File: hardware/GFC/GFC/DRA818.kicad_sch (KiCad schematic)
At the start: 24 parts, among them J3 USB Sound Card Connection, Q2 DMN67D8LW-13, Q3 Q_NPN_BCE, SW1 H/L_DIP_SW

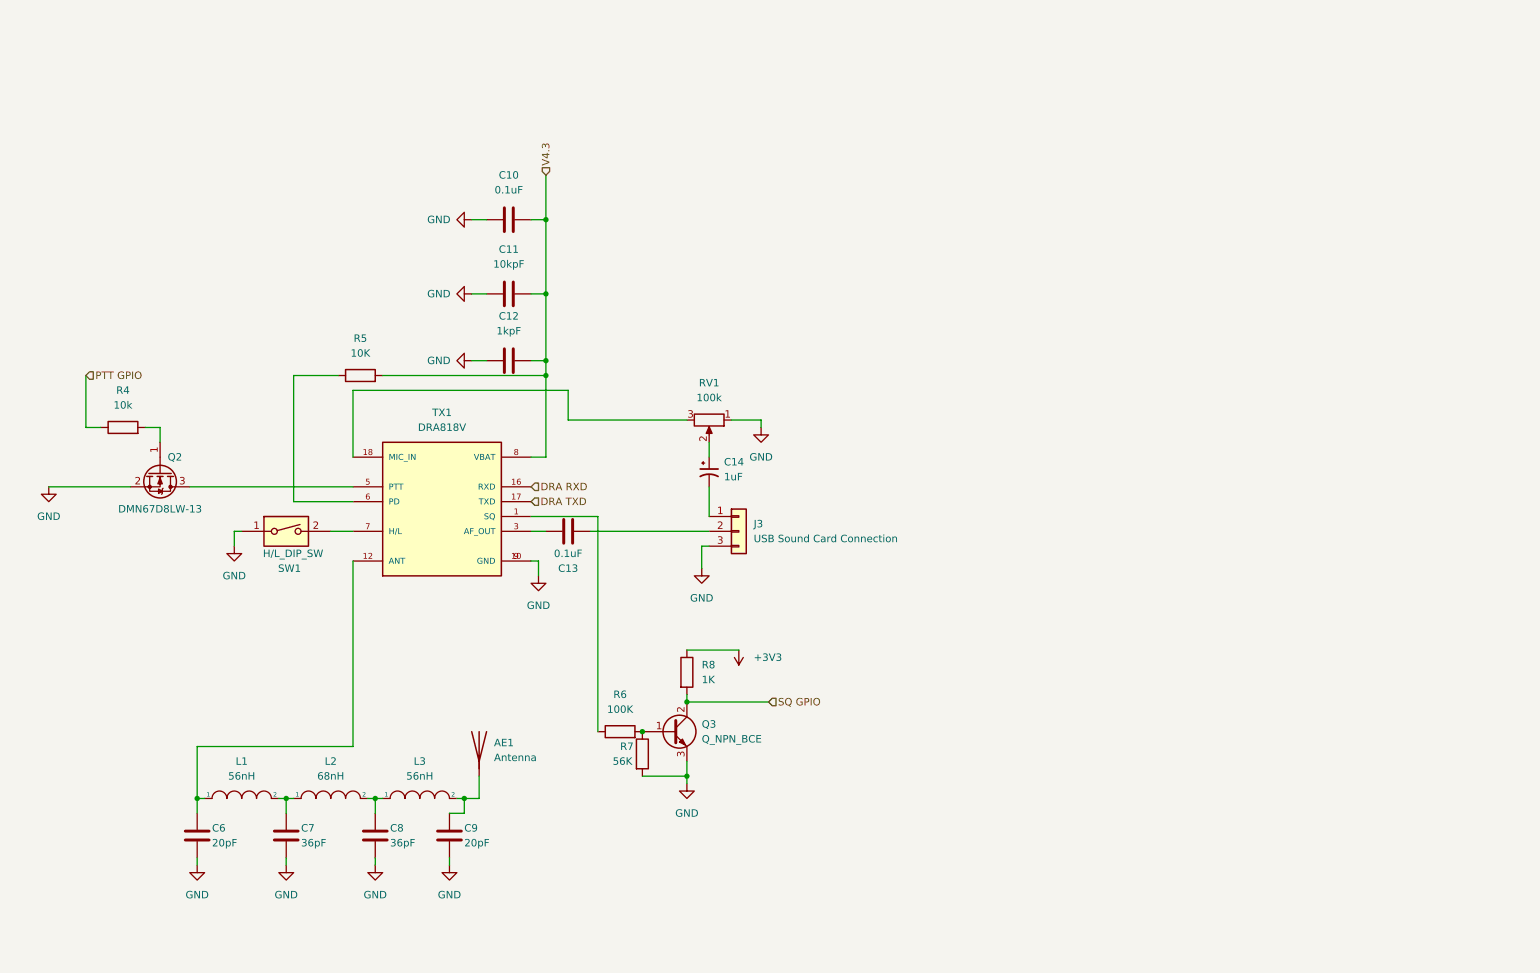
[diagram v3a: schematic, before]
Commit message: Schematic Update - ADC/DAC & GPIO Config EEPROM
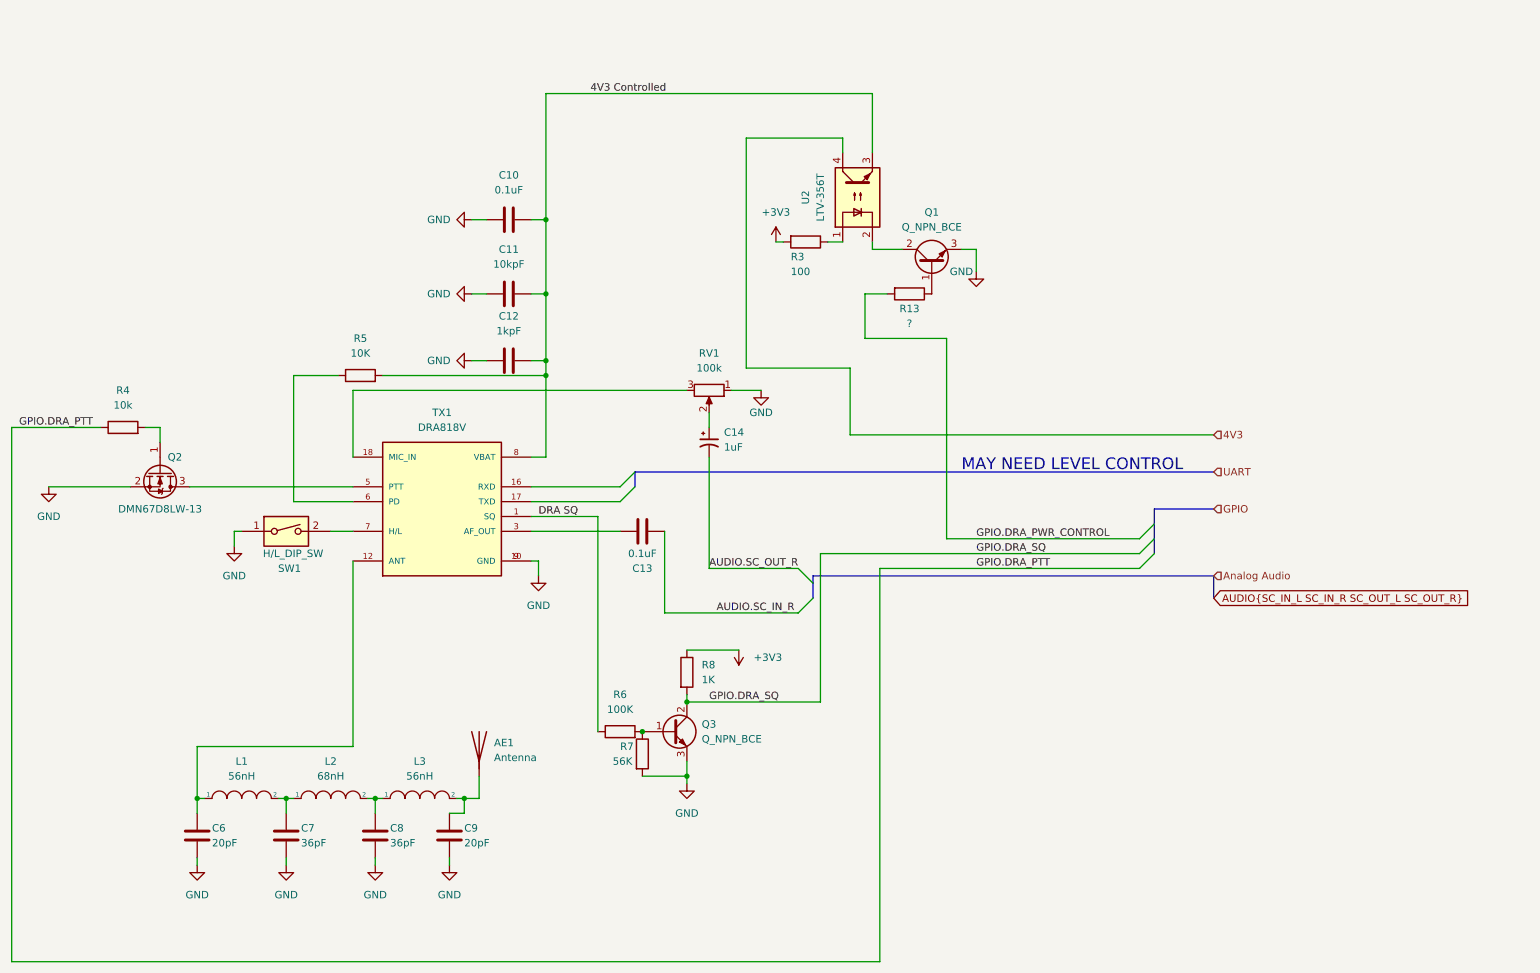
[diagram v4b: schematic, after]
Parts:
- removed J3: USB Sound Card Connection, Connector_PinHeader_2.54mm:PinHeader_1x03_P2.54mm_Vertical, symbol Connector_Generic:Conn_01x03
- added Q1: Q_NPN_BCE, Package_TO_SOT_SMD:SOT-23, symbol Device:Q_NPN_BCE
- added R13: ?, Resistor_SMD:R_0603_1608Metric_Pad0.98x0.95mm_HandSolder, symbol Device:R
- added R3: 100, Resistor_SMD:R_0805_2012Metric_Pad1.20x1.40mm_HandSolder, symbol Device:R
- added U2: LTV-356T, Package_SO:SO-4_4.4x3.6mm_P2.54mm, symbol Isolator:LTV-356T
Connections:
- net +3V3: now also R3.2
- net GND: now also Q1.3 (E)
- net AUDIO.SC_IN_R: now reaches C13.2
- net AUDIO.SC_OUT_R: now reaches C14.2
- net DRA SQ: now reaches R6.1, TX1.1 (SQ)
- net DRA RXD: no longer names the net of TX1.16 (RXD)
- net DRA TXD: no longer names the net of TX1.17 (TXD)
- net PTT GPIO renamed GPIO.DRA_PTT
- net SQ GPIO renamed GPIO.DRA_SQ
- net V4.3 renamed 4V3 Controlled
- net 4V3 Controlled: now also U2.3
- new net: Q1.1 (B), R13.1
- new net: Q1.2 (C), U2.2
- new net: R3.1, U2.1
- new net 4V3: U2.4
- new net GPIO.DRA_PWR_CONTROL: R13.2
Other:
- note added: "MAY NEED LEVEL CONTROL"
- moved on the sheet: C13, C14, RV1

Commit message: sync
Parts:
- added TP1, TP19, TP20, TP21, TP22, TP23, TP24, TP25, TP26, TP27, TP28: Test Point, TestPoint:TestPoint_Pad_D1.0mm, symbol Connector:TestPoint_Small
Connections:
- net 4V3: now also TP26.1
- net 4V3 Controlled: now also TP22.1, TP27.1
- net AUDIO.SC_OUT_R: now also RV1.2, TP25.1; no longer C14.2
- net DRA SQ: now also TP23.1
- net at Q1.2 (C), U2.2: now also TP28.1
- net at C13.1, TX1.3 (AF_OUT): now also TP21.1
- net at C14.1: now also RV1.3, TP24.1; no longer RV1.2
- net at TX1.18 (MIC_IN): now also C14.2; no longer RV1.3
- net at R5.1, TX1.6 (PD): now also TP20.1
- net at Q2.1 (G), R4.2: now also TP1.1
- net at Q2.3 (D), TX1.5 (PTT): now also TP19.1
- net UART0.PI_TXD: now reaches TX1.16 (RXD)
- net UART0.PI_RXD: now reaches TX1.17 (TXD)
